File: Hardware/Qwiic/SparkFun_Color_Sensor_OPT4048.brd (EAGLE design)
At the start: 25.4 x 25.4 mm, 53 parts, among them J1 QWIIC_RIGHT_ANGLE, J2 QWIIC_RIGHT_ANGLE, U1 OPT4048

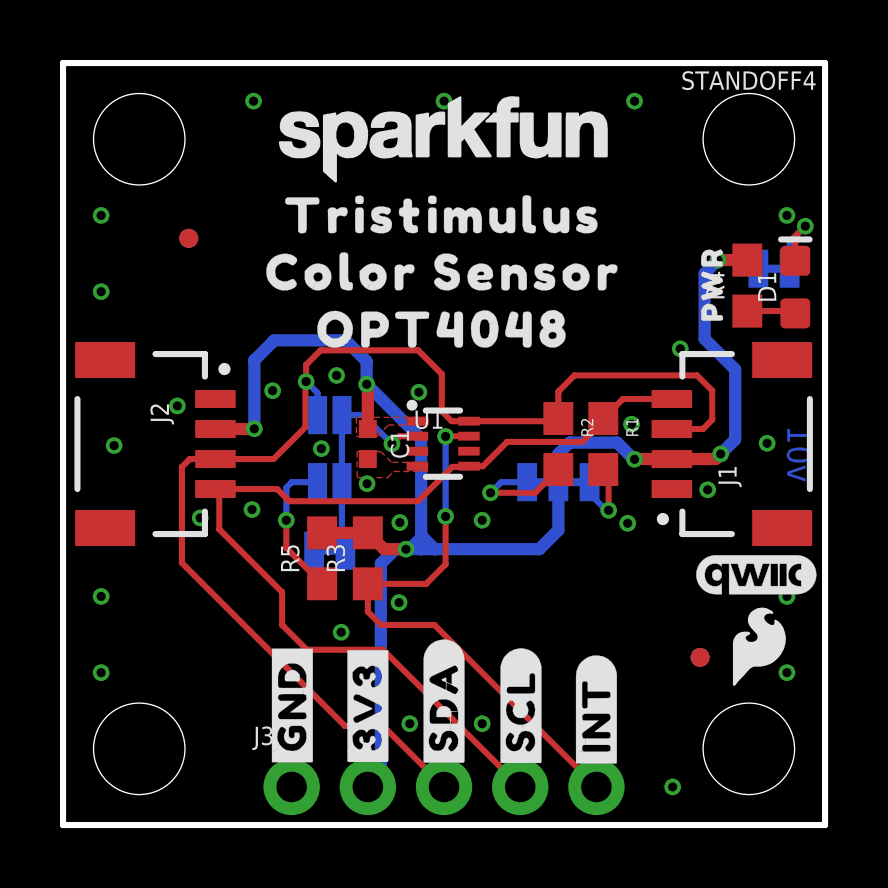
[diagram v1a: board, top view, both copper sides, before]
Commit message: Adds correct red LEDs and their resistors, updates PROD_ID for part.
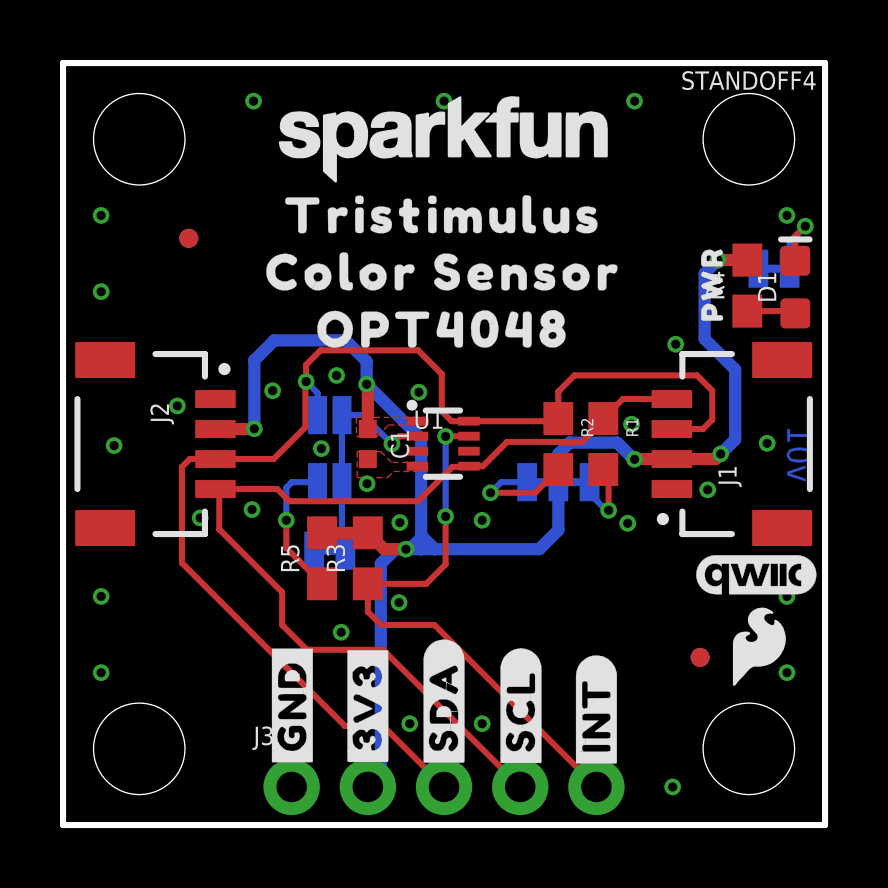
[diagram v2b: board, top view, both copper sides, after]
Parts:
- R4: value 1k -> 4.7k
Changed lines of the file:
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@@
 <layer number="39" name="tKeepout" color="4" fill="11" visible="no" active="yes"/>
 <layer number="40" name="bKeepout" color="1" fill="11" visible="no" active="yes"/>
-<layer number="41" name="tRestrict" color="4" fill="10" visible="yes" active="yes"/>
+<layer number="41" name="tRestrict" color="4" fill="10" visible="no" active="yes"/>
 <layer number="42" name="bRestrict" color="1" fill="10" visible="no" active="yes"/>
 <layer number="43" name="vRestrict" color="2" fill="10" visible="no" active="yes"/>
@@
 <element name="D1" library="SparkFun-LED" package="LED-0603" value="RED" x="24.4094" y="17.9324" smashed="yes" rot="R90">
 <attribute name="NAME" x="23.7744" y="17.9324" size="0.6096" layer="25" font="vector" ratio="20" rot="R90" align="bottom-center"/>
-<attribute name="PROD_ID" value="DIO-00819" x="24.4094" y="17.9324" size="1.778" layer="27" rot="R90" display="off"/>
-<attribute name="VALUE" value="RED" x="25.0444" y="17.9324" size="0.6096" layer="27" font="vector" ratio="20" rot="R90" align="top-center"/>
-</element>
-<element name="R4" library="SparkFun-Resistors" package="0603" value="1k" x="22.8092" y="17.9832" smashed="yes" rot="R90">
+<attribute name="PROD_ID" value="DIO-17976" x="24.4094" y="17.9324" size="1.778" layer="27" rot="R90" display="off"/>
+</element>
+<element name="R4" library="SparkFun-Resistors" package="0603" value="4.7k" x="22.8092" y="17.9832" smashed="yes" rot="R90">
 <attribute name="NAME" x="22.0472" y="17.9832" size="0.6096" layer="25" font="vector" ratio="20" rot="R90" align="bottom-center"/>
-<attribute name="PROD_ID" value="RES-07856" x="22.8092" y="17.9832" size="1.778" layer="27" font="vector" ratio="15" rot="R90" display="off"/>
-<attribute name="VALUE" x="23.5712" y="17.9832" size="0.6096" layer="27" font="vector" ratio="20" rot="R90" align="top-center"/>
+<attribute name="PROD_ID" value="RES-07857" x="22.8092" y="17.9832" size="1.778" layer="27" font="vector" ratio="15" rot="R90" display="off"/>
+<attribute name="VALUE" value="4.7k" x="23.5712" y="17.9832" size="0.6096" layer="27" font="vector" ratio="20" rot="R90" align="top-center"/>
 </element>
 <element name="LED" library="SparkFun-Jumpers" package="SMT-JUMPER_2_NC_TRACE_SILK" package3d_urn="urn:adsk.eagle:package:39281/1" value="JUMPER-SMT_2_NC_TRACE_SILK" x="23.6982" y="18.542" smashed="yes" rot="MR180">
@@
 <via x="21.4884" y="11.176" extent="1-16" drill="0.3048"/>
 <via x="4.572" y="10.2362" extent="1-16" drill="0.3048"/>
-<via x="20.574" y="15.875" extent="1-16" drill="0.3048"/>
+<via x="20.4216" y="16.0274" extent="1-16" drill="0.3048"/>
 <via x="3.81" y="13.97" extent="1-16" drill="0.3048"/>
 <via x="6.985" y="14.478" extent="1-16" drill="0.3048"/>
